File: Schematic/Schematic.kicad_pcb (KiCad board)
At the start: 2 copper layers, 249.9 x 89.4 mm, 55 parts, among them IC1 AS6C62256, IC10 74LS593, IC11 74LS251-RESCUE-Schematic, IC12 74HCT574, IC13 74HCT161, IC14 AT27C1024-70PU, IC15 74HCT139, IC16 74HCT138, IC17 74HCT04, IC18 NE555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

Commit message: Updated the PCB so that the UM245R has the correct physical orientation with the USB port facing the edge of the PCB.
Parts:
- moved IC3 36.8 mm to (266.2, 72.8), turned to 180 degrees
- moved C3 18.7 mm to (244.7, 65.2), turned to 180 degrees
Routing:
- net ~UARTresult: track 153.6 -> 250.0 mm
- net d2: track 253.2 -> 331.0 mm, vias 2 -> 1
- net d0: track 289.0 -> 337.6 mm
- net d7: track 236.2 -> 268.1 mm, vias 0 -> 2
- net d6: track 235.2 -> 267.1 mm, vias 0 -> 2
- net Net-(IC12-Pad13): track 70.4 -> 100.0 mm
- net adr5: track 133.0 -> 160.8 mm, vias 2 -> 1
- net adr6: track 130.5 -> 151.4 mm
- net d5: track 251.2 -> 271.7 mm, vias 0 -> 1
- net d3: track 267.4 -> 287.6 mm, vias 4 -> 2
- net adr15: track 199.5 -> 217.6 mm, vias 1 -> 0
- net ~uSreset: track 73.6 -> 90.9 mm, vias 1 -> 0
- net Lo: track 986.5 -> 970.6 mm
- net ~ARena: track 200.6 -> 216.0 mm, vias 0 -> 2
- net ~MEMload: track 82.4 -> 96.6 mm
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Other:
- board text added: "v2019/05/25"
- board text removed: "v2019/05/08"

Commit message: Updated the PCB and schematic to have a 330pF capacitor to fix the "jump" glitch that I've been experiencing.
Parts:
- added C2: 330pF, Capacitor_THT:C_Disc_D4.7mm_W2.5mm_P5.00mm, F.Cu at (72.9, 101.6)
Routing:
- net d1: track 280.9 -> 332.0 mm
- net d2: track 331.0 -> 285.1 mm, vias 1 -> 2
- net d0: track 337.6 -> 292.2 mm, vias 1 -> 2
- net Hi: track 697.3 -> 652.5 mm, vias 0 -> 1
- net Net-(IC12-Pad13): track 100.0 -> 56.8 mm, vias 0 -> 1
- net ~UARTresult: track 250.0 -> 218.5 mm
- net Net-(IC5-Pad19): track 69.1 -> 97.1 mm
- net adr10: track 198.2 -> 171.3 mm, vias 0 -> 1
- net ~RXready: track 131.6 -> 106.0 mm, vias 0 -> 1
- net adr7: track 159.6 -> 134.3 mm, vias 0 -> 1
- net ~ARena: track 216.0 -> 191.9 mm, vias 2 -> 0
- net adr5: track 160.8 -> 137.8 mm, vias 1 -> 0
- net d3: track 287.6 -> 308.6 mm, vias 2 -> 3
- net ~uSreset: track 90.9 -> 73.2 mm, vias 0 -> 1
- net d5: track 271.7 -> 286.2 mm, vias 1 -> 2
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
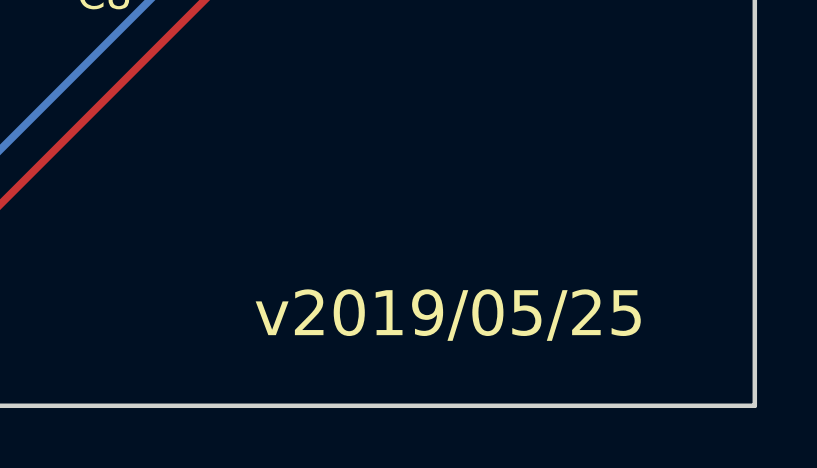
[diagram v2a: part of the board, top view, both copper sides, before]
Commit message: Changed the version number on the PCB to reflect the new capacitor.
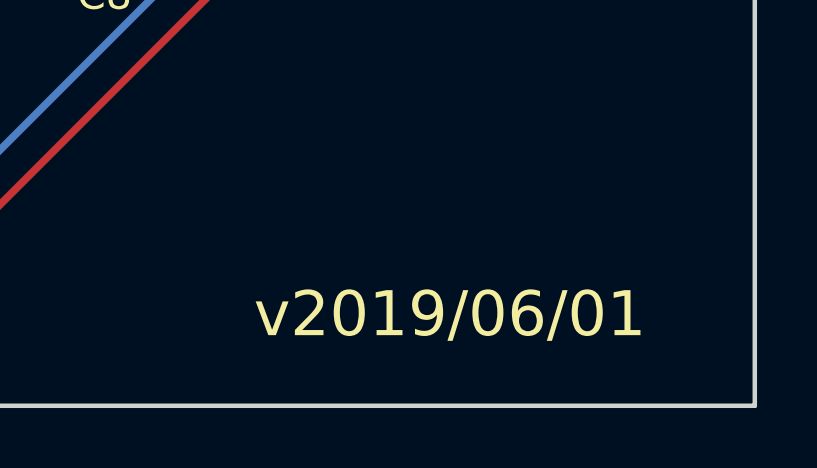
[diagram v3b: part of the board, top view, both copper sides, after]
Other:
- board text added: "v2019/06/01"
- board text removed: "v2019/05/25"
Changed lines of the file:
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@@
   (gr_line (start 271.272 120.904) (end 21.336 120.904) (angle 90) (layer Edge.Cuts) (width 0.15))
   (gr_line (start 271.272 31.496) (end 271.272 120.904) (angle 90) (layer Edge.Cuts) (width 0.15))
-  (gr_text v2019/05/25 (at 261.112 117.856) (layer F.SilkS)
+  (gr_text v2019/06/01 (at 261.112 117.856) (layer F.SilkS)
     (effects (font (size 1.5 1.5) (thickness 0.3)))
   )

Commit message: I've updated the schematic and the PCB to have the 74HCT151 chip.
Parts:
- removed C2: 330pF, Capacitor_THT:C_Disc_D4.7mm_W2.5mm_P5.00mm
- IC11: value 74LS251-RESCUE-Schematic -> 74HCT151
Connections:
- IC11 pad 7: Lo -> Clk
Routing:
- net Hi: track 652.5 -> 756.5 mm, vias 1 -> 0
- net d1: track 332.0 -> 289.3 mm, vias 1 -> 3
- net PCincr: track 135.0 -> 167.2 mm
- net Net-(IC5-Pad19): track 97.1 -> 69.1 mm
- net adr3: track 113.2 -> 138.7 mm, vias 0 -> 1
- net d3: track 308.6 -> 286.6 mm, vias 3 -> 2
- net ~RXready: track 106.0 -> 127.5 mm, vias 1 -> 0
- net adr4: track 145.7 -> 124.2 mm, vias 1 -> 0
- net adr2: track 112.4 -> 131.6 mm, vias 0 -> 1
- net d5: track 286.2 -> 267.3 mm, vias 2 -> 1
- net d0: track 292.2 -> 310.3 mm, vias 2 -> 1
- net adr10: track 171.3 -> 186.9 mm, vias 1 -> 0
- net ~uSreset: track 73.2 -> 87.2 mm, vias 1 -> 0
- net Op4: track 62.9 -> 75.4 mm
- net ~UARTresult: track 218.5 -> 207.6 mm
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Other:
- board text added: "v2019/06/07"
- board text removed: "v2019/06/01"
